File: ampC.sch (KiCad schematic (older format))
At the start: 9 parts, among them U3 MCP6004, U7 Mux

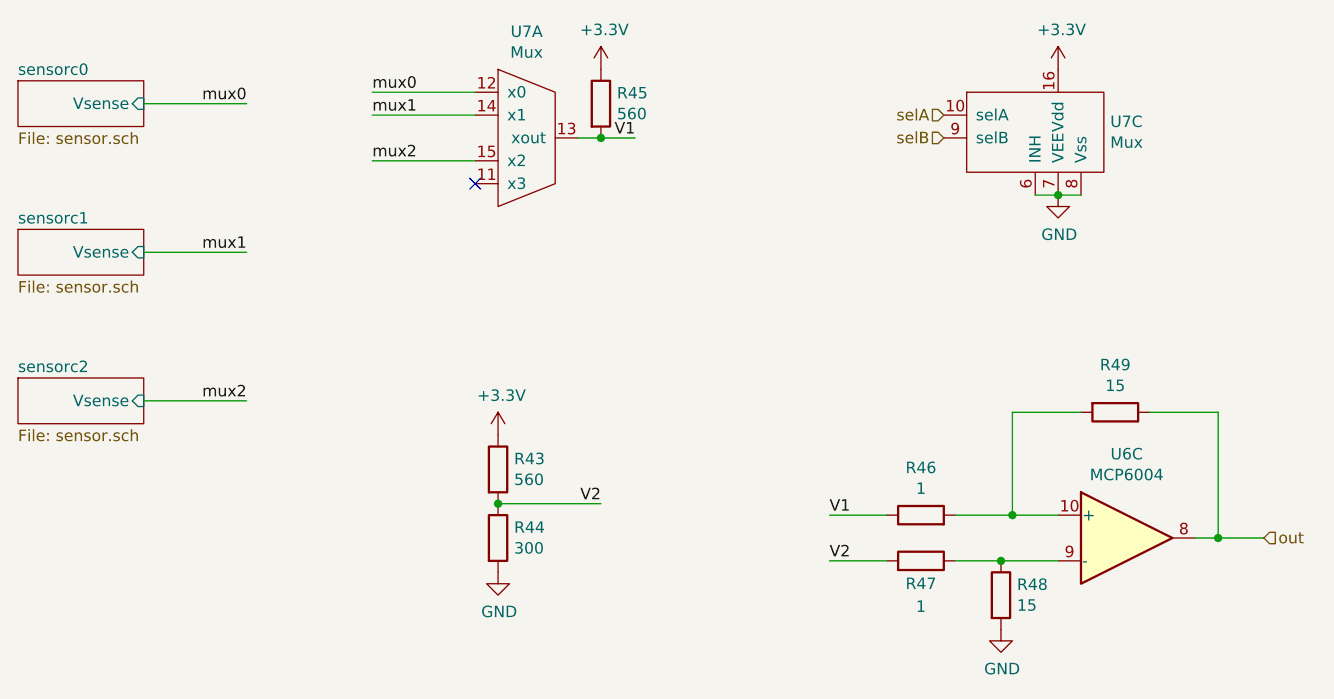
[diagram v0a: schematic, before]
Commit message: changed to 1.00mm screw term holes
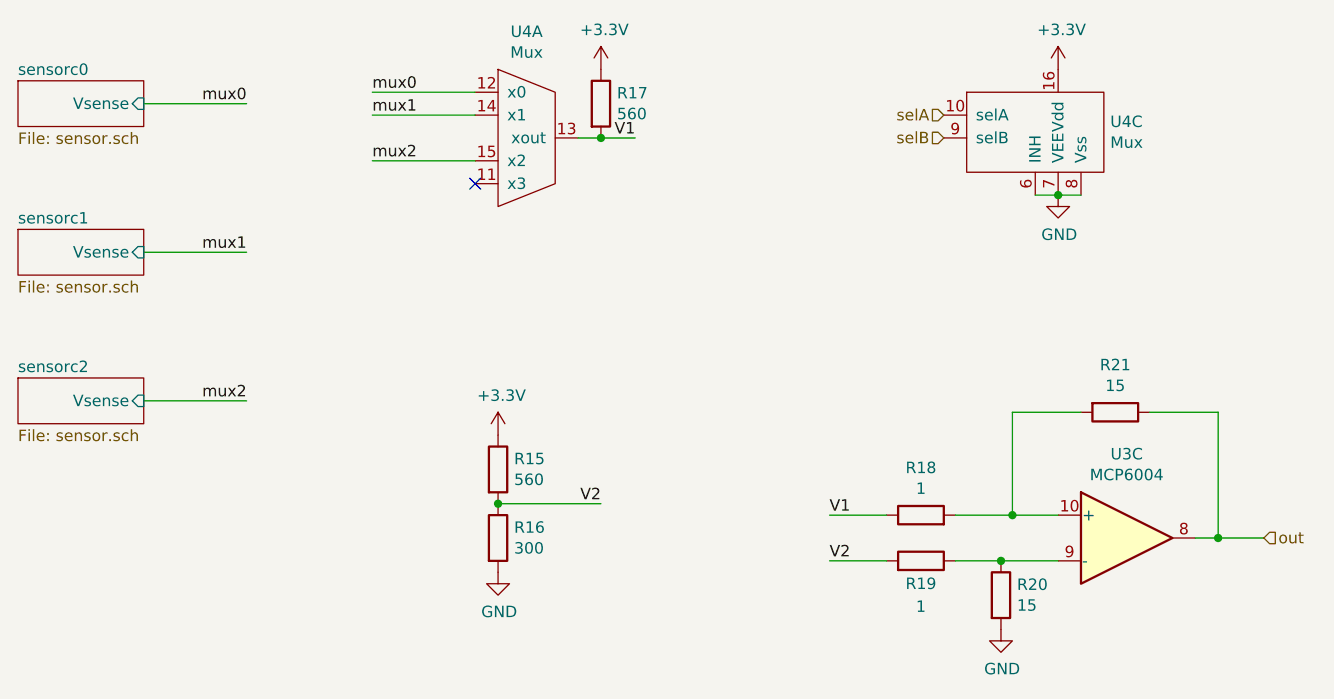
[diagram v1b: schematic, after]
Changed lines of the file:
@@
 AR Path="/6019C043/60198F28" Ref="R20"  Part="1"
 AR Path="/601B4C16/60198F28" Ref="R48"  Part="1"
-F 0 "R48" H 5520 4096 50  0000 L CNN
+F 0 "R20" H 5520 4096 50  0000 L CNN
 F 1 "15" H 5520 4005 50  0000 L CNN
 F 2 "Resistor_SMD:R_0805_2012Metric_Pad1.20x1.40mm_HandSolder" V 5380 4050 50  0001 C CNN
@@
 AR Path="/6019C043/6019D567" Ref="R21"  Part="1"
 AR Path="/601B4C16/6019D567" Ref="R49"  Part="1"
-F 0 "R49" V 5743 3250 50  0000 C CNN
+F 0 "R21" V 5743 3250 50  0000 C CNN
 F 1 "15" V 5834 3250 50  0000 C CNN
 F 2 "Resistor_SMD:R_0805_2012Metric_Pad1.20x1.40mm_HandSolder" V 5880 3250 50  0001 C CNN
@@
 AR Path="/6019C043/6019D55D" Ref="R18"  Part="1"
 AR Path="/601B4C16/6019D55D" Ref="R46"  Part="1"
-F 0 "R46" V 5307 3700 50  0000 C CNN
+F 0 "R18" V 5307 3700 50  0000 C CNN
 F 1 "1" V 5216 3700 50  0000 C CNN
 F 2 "Resistor_SMD:R_0805_2012Metric_Pad1.20x1.40mm_HandSolder" V 5030 3700 50  0001 C CNN
@@
 AR Path="/6019C043/60198F34" Ref="R19"  Part="1"
 AR Path="/601B4C16/60198F34" Ref="R47"  Part="1"
-F 0 "R47" V 5000 3900 50  0000 C CNN
+F 0 "R19" V 5000 3900 50  0000 C CNN
 F 1 "1" V 4900 3900 50  0000 C CNN
 F 2 "Resistor_SMD:R_0805_2012Metric_Pad1.20x1.40mm_HandSolder" V 5030 3900 50  0001 C CNN
@@
 AR Path="/6019C043/6017E433" Ref="R15"  Part="1"
 AR Path="/601B4C16/6017E433" Ref="R43"  Part="1"
-F 0 "R43" H 3320 3546 50  0000 L CNN
+F 0 "R15" H 3320 3546 50  0000 L CNN
 F 1 "560" H 3320 3455 50  0000 L CNN
 F 2 "Resistor_SMD:R_0805_2012Metric_Pad1.20x1.40mm_HandSolder" V 3180 3500 50  0001 C CNN
@@
 AR Path="/6019C043/6017E434" Ref="R16"  Part="1"
 AR Path="/601B4C16/6017E434" Ref="R44"  Part="1"
-F 0 "R44" H 3320 3846 50  0000 L CNN
+F 0 "R16" H 3320 3846 50  0000 L CNN
 F 1 "300" H 3320 3755 50  0000 L CNN
 F 2 "Resistor_SMD:R_0805_2012Metric_Pad1.20x1.40mm_HandSolder" V 3180 3800 50  0001 C CNN
@@
 AR Path="/6019C043/6017E435" Ref="#PWR026"  Part="1"
 AR Path="/601B4C16/6017E435" Ref="#PWR060"  Part="1"
-F 0 "#PWR060" H 3250 3200 50  0001 C CNN
+F 0 "#PWR026" H 3250 3200 50  0001 C CNN
 F 1 "+3.3V" H 3265 3523 50  0000 C CNN
 F 2 "" H 3250 3350 50  0001 C CNN
@@
 AR Path="/6019C043/6019D569" Ref="#PWR027"  Part="1"
 AR Path="/601B4C16/6019D569" Ref="#PWR061"  Part="1"
-F 0 "#PWR061" H 3250 3700 50  0001 C CNN
+F 0 "#PWR027" H 3250 3700 50  0001 C CNN
 F 1 "GND" H 3255 3777 50  0000 C CNN
 F 2 "" H 3250 3950 50  0001 C CNN
@@
 AR Path="/6019C043/6019D555" Ref="#PWR029"  Part="1"
 AR Path="/601B4C16/6019D555" Ref="#PWR063"  Part="1"
-F 0 "#PWR063" H 5450 3950 50  0001 C CNN
+F 0 "#PWR029" H 5450 3950 50  0001 C CNN
 F 1 "GND" H 5455 4027 50  0000 C CNN
 F 2 "" H 5450 4200 50  0001 C CNN
@@
 AR Path="/6019C043/6019D563" Ref="#PWR031"  Part="1"
 AR Path="/601B4C16/6019D563" Ref="#PWR065"  Part="1"
-F 0 "#PWR065" H 5700 2050 50  0001 C CNN
+F 0 "#PWR031" H 5700 2050 50  0001 C CNN
 F 1 "GND" H 5705 2127 50  0000 C CNN
 F 2 "" H 5700 2300 50  0001 C CNN
@@
 AR Path="/6019C043/6019D564" Ref="#PWR030"  Part="1"
 AR Path="/601B4C16/6019D564" Ref="#PWR064"  Part="1"
-F 0 "#PWR064" H 5700 1600 50  0001 C CNN
+F 0 "#PWR030" H 5700 1600 50  0001 C CNN
 F 1 "+3.3V" H 5715 1923 50  0000 C CNN
 F 2 "" H 5700 1750 50  0001 C CNN
@@
 AR Path="/601B4C16/601763C1" Ref="U7"  Part="1"
 AR Path="/6019C043/601763C1" Ref="U4"  Part="1"
-F 0 "U7" H 3375 2515 50  0000 C CNN
+F 0 "U4" H 3375 2515 50  0000 C CNN
 F 1 "Mux" H 3375 2424 50  0000 C CNN
 F 2 "Package_SO:SOIC-16_3.9x9.9mm_P1.27mm" H 3350 2050 50  0001 C CNN
@@
 AR Path="/601B4C16/60176BAF" Ref="U7"  Part="3"
 AR Path="/6019C043/60176BAF" Ref="U4"  Part="3"
-F 0 "U7" H 5928 2221 50  0000 L CNN
+F 0 "U4" H 5928 2221 50  0000 L CNN
 F 1 "Mux" H 5928 2130 50  0000 L CNN
 F 2 "Package_SO:SOIC-16_3.9x9.9mm_P1.27mm" H 5700 2100 50  0001 C CNN
@@
 AR Path="/6019C043/6018DE62" Ref="U3"  Part="3"
 AR Path="/601B4C16/6018DE62" Ref="U6"  Part="3"
-F 0 "U6" H 6000 4167 50  0000 C CNN
+F 0 "U3" H 6000 4167 50  0000 C CNN
 F 1 "MCP6004" H 6000 4076 50  0000 C CNN
 F 2 "Package_SO:SOIC-14_3.9x8.7mm_P1.27mm" H 5950 3900 50  0001 C CNN
@@
 AR Path="/6019C043/60205F03" Ref="R17"  Part="1"
 AR Path="/601B4C16/60205F03" Ref="R45"  Part="1"
-F 0 "R45" H 3770 1946 50  0000 L CNN
+F 0 "R17" H 3770 1946 50  0000 L CNN
 F 1 "560" H 3770 1855 50  0000 L CNN
 F 2 "Resistor_SMD:R_0805_2012Metric_Pad1.20x1.40mm_HandSolder" V 3630 1900 50  0001 C CNN
@@
 AR Path="/6019C043/60206022" Ref="#PWR028"  Part="1"
 AR Path="/601B4C16/60206022" Ref="#PWR062"  Part="1"
-F 0 "#PWR062" H 3700 1600 50  0001 C CNN
+F 0 "#PWR028" H 3700 1600 50  0001 C CNN
 F 1 "+3.3V" H 3715 1923 50  0000 C CNN
 F 2 "" H 3700 1750 50  0001 C CNN

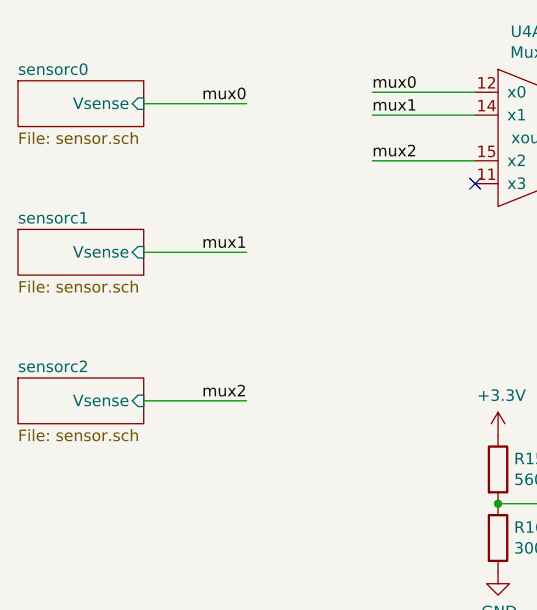
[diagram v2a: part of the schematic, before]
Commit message: updated sch with pico connectors
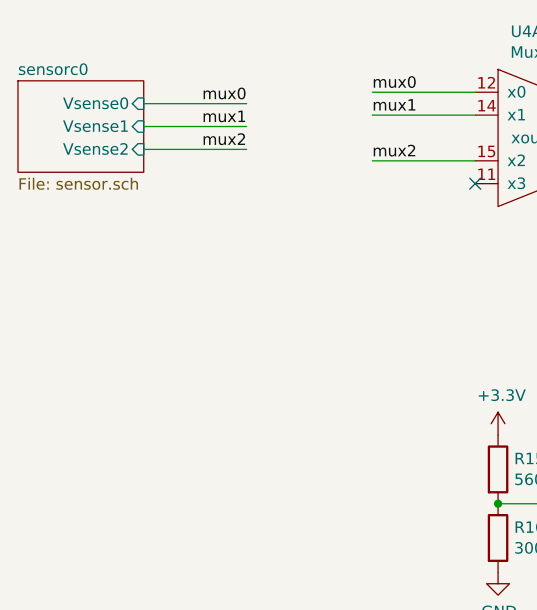
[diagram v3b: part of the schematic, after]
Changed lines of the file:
@@
 $Descr A4 11693 8268
 encoding utf-8
-Sheet 10 41
+Sheet 6 21
 Title ""
 Date ""
@@
 AR Path="/6019C043/6017E435" Ref="#PWR026"  Part="1"
 AR Path="/601B4C16/6017E435" Ref="#PWR060"  Part="1"
-F 0 "#PWR060" H 3250 3200 50  0001 C CNN
+F 0 "#PWR026" H 3250 3200 50  0001 C CNN
 F 1 "+3.3V" H 3265 3523 50  0000 C CNN
 F 2 "" H 3250 3350 50  0001 C CNN
@@
 AR Path="/6019C043/6019D569" Ref="#PWR027"  Part="1"
 AR Path="/601B4C16/6019D569" Ref="#PWR061"  Part="1"
-F 0 "#PWR061" H 3250 3700 50  0001 C CNN
+F 0 "#PWR027" H 3250 3700 50  0001 C CNN
 F 1 "GND" H 3255 3777 50  0000 C CNN
 F 2 "" H 3250 3950 50  0001 C CNN
@@
 AR Path="/6019C043/6019D555" Ref="#PWR029"  Part="1"
 AR Path="/601B4C16/6019D555" Ref="#PWR063"  Part="1"
-F 0 "#PWR063" H 5450 3950 50  0001 C CNN
+F 0 "#PWR029" H 5450 3950 50  0001 C CNN
 F 1 "GND" H 5455 4027 50  0000 C CNN
 F 2 "" H 5450 4200 50  0001 C CNN
@@
 AR Path="/6019C043/6019D563" Ref="#PWR031"  Part="1"
 AR Path="/601B4C16/6019D563" Ref="#PWR065"  Part="1"
-F 0 "#PWR065" H 5700 2050 50  0001 C CNN
+F 0 "#PWR031" H 5700 2050 50  0001 C CNN
 F 1 "GND" H 5705 2127 50  0000 C CNN
 F 2 "" H 5700 2300 50  0001 C CNN
@@
 AR Path="/6019C043/6019D564" Ref="#PWR030"  Part="1"
 AR Path="/601B4C16/6019D564" Ref="#PWR064"  Part="1"
-F 0 "#PWR064" H 5700 1600 50  0001 C CNN
+F 0 "#PWR030" H 5700 1600 50  0001 C CNN
 F 1 "+3.3V" H 5715 1923 50  0000 C CNN
 F 2 "" H 5700 1750 50  0001 C CNN
@@
 mux0
 $Sheet
-S 1150 1800 550  200
+S 1150 1800 550  400
 U 601A47AA
 F0 "sensorc0" 50
 F1 "sensor.sch" 50
-F2 "Vsense" I R 1700 1900 50
+F2 "Vsense0" I R 1700 1900 50
+F3 "Vsense1" I R 1700 2000 50
+F4 "Vsense2" I R 1700 2100 50
 $EndSheet
-Wire Wire Line
-	1700 2550 2150 2550
-Text Label 2150 2550 2    50   ~ 0
+Text Label 2150 2000 2    50   ~ 0
 mux1
-$Sheet
-S 1150 2450 550  200
-U 601A47AF
-F0 "sensorc1" 50
-F1 "sensor.sch" 50
-F2 "Vsense" I R 1700 2550 50
-$EndSheet
-Wire Wire Line
-	1700 3200 2150 3200
-Text Label 2150 3200 2    50   ~ 0
+Text Label 2150 2100 2    50   ~ 0
 mux2
-$Sheet
-S 1150 3100 550  200
-U 601A47B4
-F0 "sensorc2" 50
-F1 "sensor.sch" 50
-F2 "Vsense" I R 1700 3200 50
-$EndSheet
 $Comp
 L Device:R R?
@@
 AR Path="/6019C043/60206022" Ref="#PWR028"  Part="1"
 AR Path="/601B4C16/60206022" Ref="#PWR062"  Part="1"
-F 0 "#PWR062" H 3700 1600 50  0001 C CNN
+F 0 "#PWR028" H 3700 1600 50  0001 C CNN
 F 1 "+3.3V" H 3715 1923 50  0000 C CNN
 F 2 "" H 3700 1750 50  0001 C CNN
@@
 	1    0    0    -1
 $EndComp
+Wire Wire Line
+	1700 2000 2150 2000
+Wire Wire Line
+	2150 2100 1700 2100
 $EndSCHEMATC

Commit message: left off reworking bottom of board
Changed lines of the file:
@@
 AR Path="/6019C043/60198F28" Ref="R20"  Part="1"
 AR Path="/601B4C16/60198F28" Ref="R48"  Part="1"
-F 0 "R20" H 5520 4096 50  0000 L CNN
+F 0 "R48" H 5520 4096 50  0000 L CNN
 F 1 "15" H 5520 4005 50  0000 L CNN
 F 2 "Resistor_SMD:R_0805_2012Metric_Pad1.20x1.40mm_HandSolder" V 5380 4050 50  0001 C CNN
@@
 AR Path="/6019C043/6019D567" Ref="R21"  Part="1"
 AR Path="/601B4C16/6019D567" Ref="R49"  Part="1"
-F 0 "R21" V 5743 3250 50  0000 C CNN
+F 0 "R49" V 5743 3250 50  0000 C CNN
 F 1 "15" V 5834 3250 50  0000 C CNN
 F 2 "Resistor_SMD:R_0805_2012Metric_Pad1.20x1.40mm_HandSolder" V 5880 3250 50  0001 C CNN
@@
 AR Path="/6019C043/6019D55D" Ref="R18"  Part="1"
 AR Path="/601B4C16/6019D55D" Ref="R46"  Part="1"
-F 0 "R18" V 5307 3700 50  0000 C CNN
+F 0 "R46" V 5307 3700 50  0000 C CNN
 F 1 "1" V 5216 3700 50  0000 C CNN
 F 2 "Resistor_SMD:R_0805_2012Metric_Pad1.20x1.40mm_HandSolder" V 5030 3700 50  0001 C CNN
@@
 AR Path="/6019C043/60198F34" Ref="R19"  Part="1"
 AR Path="/601B4C16/60198F34" Ref="R47"  Part="1"
-F 0 "R19" V 5000 3900 50  0000 C CNN
+F 0 "R47" V 5000 3900 50  0000 C CNN
 F 1 "1" V 4900 3900 50  0000 C CNN
 F 2 "Resistor_SMD:R_0805_2012Metric_Pad1.20x1.40mm_HandSolder" V 5030 3900 50  0001 C CNN
@@
 AR Path="/6019C043/6017E433" Ref="R15"  Part="1"
 AR Path="/601B4C16/6017E433" Ref="R43"  Part="1"
-F 0 "R15" H 3320 3546 50  0000 L CNN
+F 0 "R43" H 3320 3546 50  0000 L CNN
 F 1 "560" H 3320 3455 50  0000 L CNN
 F 2 "Resistor_SMD:R_0805_2012Metric_Pad1.20x1.40mm_HandSolder" V 3180 3500 50  0001 C CNN
@@
 AR Path="/6019C043/6017E434" Ref="R16"  Part="1"
 AR Path="/601B4C16/6017E434" Ref="R44"  Part="1"
-F 0 "R16" H 3320 3846 50  0000 L CNN
+F 0 "R44" H 3320 3846 50  0000 L CNN
 F 1 "300" H 3320 3755 50  0000 L CNN
 F 2 "Resistor_SMD:R_0805_2012Metric_Pad1.20x1.40mm_HandSolder" V 3180 3800 50  0001 C CNN
@@
 AR Path="/6019C043/6017E435" Ref="#PWR026"  Part="1"
 AR Path="/601B4C16/6017E435" Ref="#PWR060"  Part="1"
-F 0 "#PWR026" H 3250 3200 50  0001 C CNN
+F 0 "#PWR060" H 3250 3200 50  0001 C CNN
 F 1 "+3.3V" H 3265 3523 50  0000 C CNN
 F 2 "" H 3250 3350 50  0001 C CNN
@@
 AR Path="/6019C043/6019D569" Ref="#PWR027"  Part="1"
 AR Path="/601B4C16/6019D569" Ref="#PWR061"  Part="1"
-F 0 "#PWR027" H 3250 3700 50  0001 C CNN
+F 0 "#PWR061" H 3250 3700 50  0001 C CNN
 F 1 "GND" H 3255 3777 50  0000 C CNN
 F 2 "" H 3250 3950 50  0001 C CNN
@@
 AR Path="/6019C043/6019D555" Ref="#PWR029"  Part="1"
 AR Path="/601B4C16/6019D555" Ref="#PWR063"  Part="1"
-F 0 "#PWR029" H 5450 3950 50  0001 C CNN
+F 0 "#PWR063" H 5450 3950 50  0001 C CNN
 F 1 "GND" H 5455 4027 50  0000 C CNN
 F 2 "" H 5450 4200 50  0001 C CNN
@@
 AR Path="/6019C043/6019D563" Ref="#PWR031"  Part="1"
 AR Path="/601B4C16/6019D563" Ref="#PWR065"  Part="1"
-F 0 "#PWR031" H 5700 2050 50  0001 C CNN
+F 0 "#PWR065" H 5700 2050 50  0001 C CNN
 F 1 "GND" H 5705 2127 50  0000 C CNN
 F 2 "" H 5700 2300 50  0001 C CNN
@@
 AR Path="/6019C043/6019D564" Ref="#PWR030"  Part="1"
 AR Path="/601B4C16/6019D564" Ref="#PWR064"  Part="1"
-F 0 "#PWR030" H 5700 1600 50  0001 C CNN
+F 0 "#PWR064" H 5700 1600 50  0001 C CNN
 F 1 "+3.3V" H 5715 1923 50  0000 C CNN
 F 2 "" H 5700 1750 50  0001 C CNN
@@
 AR Path="/601B4C16/601763C1" Ref="U7"  Part="1"
 AR Path="/6019C043/601763C1" Ref="U4"  Part="1"
-F 0 "U4" H 3375 2515 50  0000 C CNN
+F 0 "U7" H 3375 2515 50  0000 C CNN
 F 1 "Mux" H 3375 2424 50  0000 C CNN
 F 2 "Package_SO:SOIC-16_3.9x9.9mm_P1.27mm" H 3350 2050 50  0001 C CNN
@@
 AR Path="/601B4C16/60176BAF" Ref="U7"  Part="3"
 AR Path="/6019C043/60176BAF" Ref="U4"  Part="3"
-F 0 "U4" H 5928 2221 50  0000 L CNN
+F 0 "U7" H 5928 2221 50  0000 L CNN
 F 1 "Mux" H 5928 2130 50  0000 L CNN
 F 2 "Package_SO:SOIC-16_3.9x9.9mm_P1.27mm" H 5700 2100 50  0001 C CNN
@@
 AR Path="/6019C043/6018DE62" Ref="U3"  Part="3"
 AR Path="/601B4C16/6018DE62" Ref="U6"  Part="3"
-F 0 "U3" H 6000 4167 50  0000 C CNN
+F 0 "U6" H 6000 4167 50  0000 C CNN
 F 1 "MCP6004" H 6000 4076 50  0000 C CNN
 F 2 "Package_SO:SOIC-14_3.9x8.7mm_P1.27mm" H 5950 3900 50  0001 C CNN
@@
 AR Path="/6019C043/60205F03" Ref="R17"  Part="1"
 AR Path="/601B4C16/60205F03" Ref="R45"  Part="1"
-F 0 "R17" H 3770 1946 50  0000 L CNN
+F 0 "R45" H 3770 1946 50  0000 L CNN
 F 1 "560" H 3770 1855 50  0000 L CNN
 F 2 "Resistor_SMD:R_0805_2012Metric_Pad1.20x1.40mm_HandSolder" V 3630 1900 50  0001 C CNN
@@
 AR Path="/6019C043/60206022" Ref="#PWR028"  Part="1"
 AR Path="/601B4C16/60206022" Ref="#PWR062"  Part="1"
-F 0 "#PWR028" H 3700 1600 50  0001 C CNN
+F 0 "#PWR062" H 3700 1600 50  0001 C CNN
 F 1 "+3.3V" H 3715 1923 50  0000 C CNN
 F 2 "" H 3700 1750 50  0001 C CNN
